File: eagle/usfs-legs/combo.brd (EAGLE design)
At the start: 35.8 x 76.9 mm, 22 parts

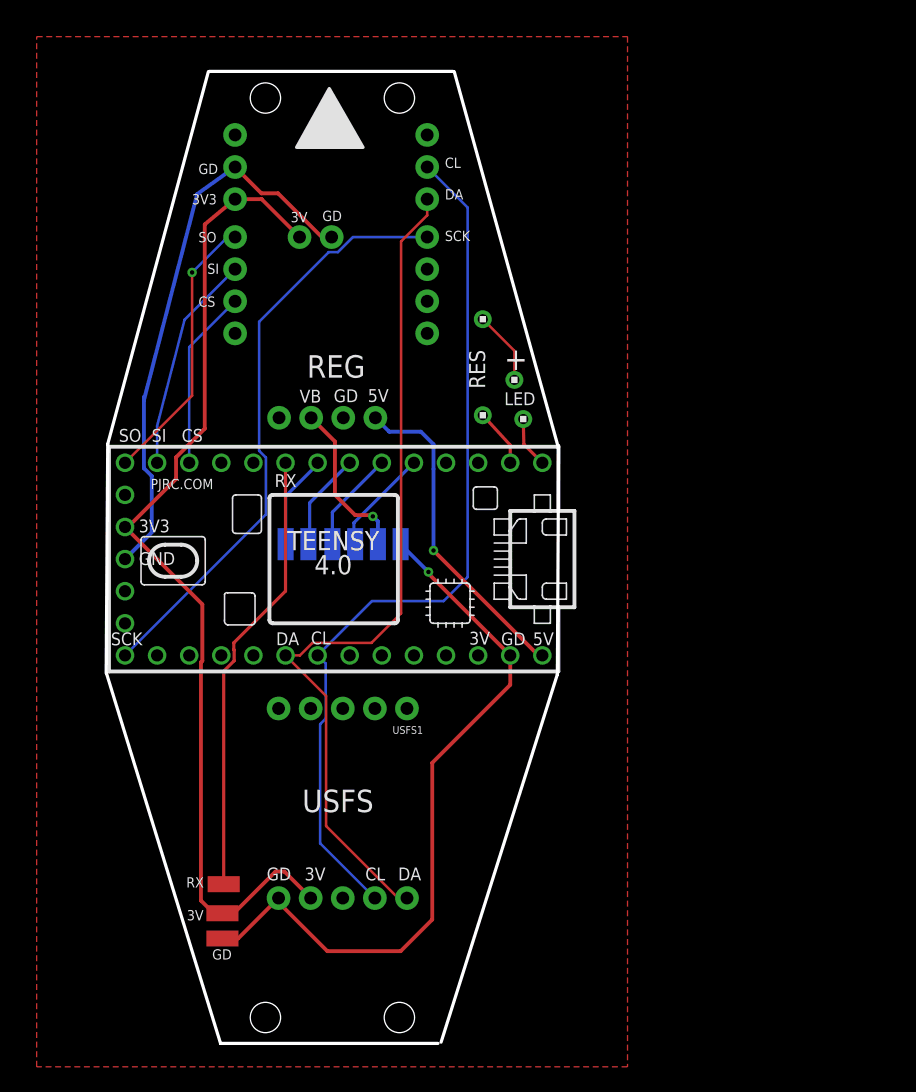
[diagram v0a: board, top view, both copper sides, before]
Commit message: modified:   eagle/usfs-legs/combo.brd
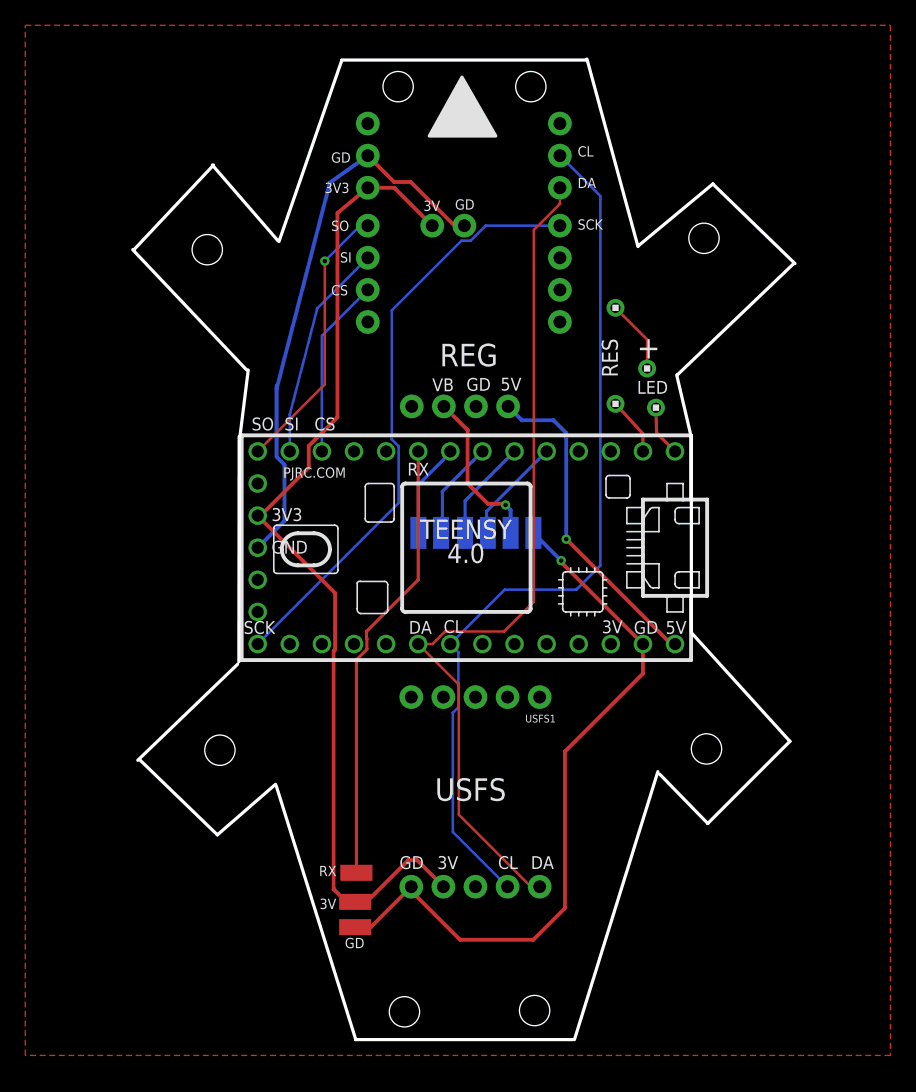
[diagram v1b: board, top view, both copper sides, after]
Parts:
- moved M2 10.5 mm to (32.7, 41.1)
- moved U$1 10.5 mm to (34.7, 39.9)
- moved VBAT 10.5 mm to (38.2, 41.1)
- moved PMW1 10.5 mm to (42.1, 65.4)
- moved PMW2 10.5 mm to (26.9, 65.4)
- moved PMW3 10.5 mm to (32.0, 65.4)
- moved USFS 10.5 mm to (40.5, 13.1)
- moved USFS1 10.5 mm to (40.5, 28.1)
- moved VL1 10.5 mm to (42.1, 68.4)
- moved VL2 10.5 mm to (26.9, 68.4)
- moved 3V 10.5 mm to (25.9, 11.9)
- moved GD 10.5 mm to (25.9, 9.90)
- moved GND 10.5 mm to (40.0, 41.1)
- moved M1 10.5 mm to (30.9, 41.1)
- moved M3 10.5 mm to (34.6, 41.1)
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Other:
- board size 35.8 x 76.9 mm -> 52.4 x 77.6 mm
